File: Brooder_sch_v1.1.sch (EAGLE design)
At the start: 37 parts, among them J2 1X2-3.5MM, J4 1X2-3.5MM, T1 2N2222, U1 328P

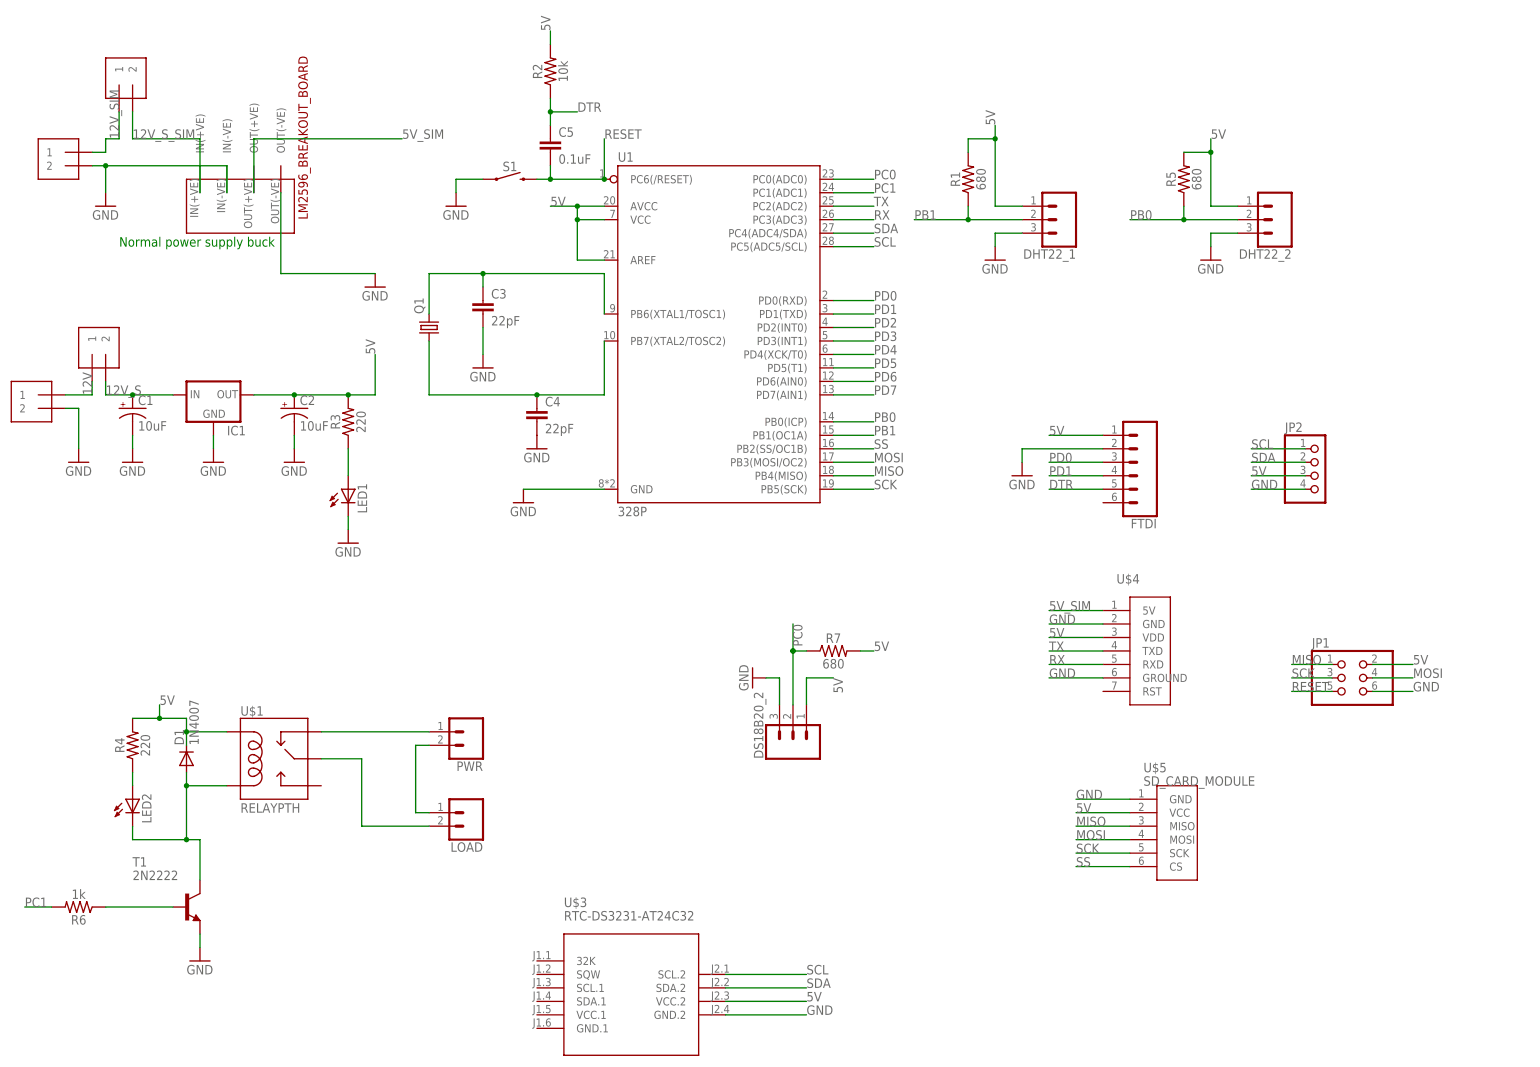
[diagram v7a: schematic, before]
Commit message: Switches the signal and ground signals for all the sensors
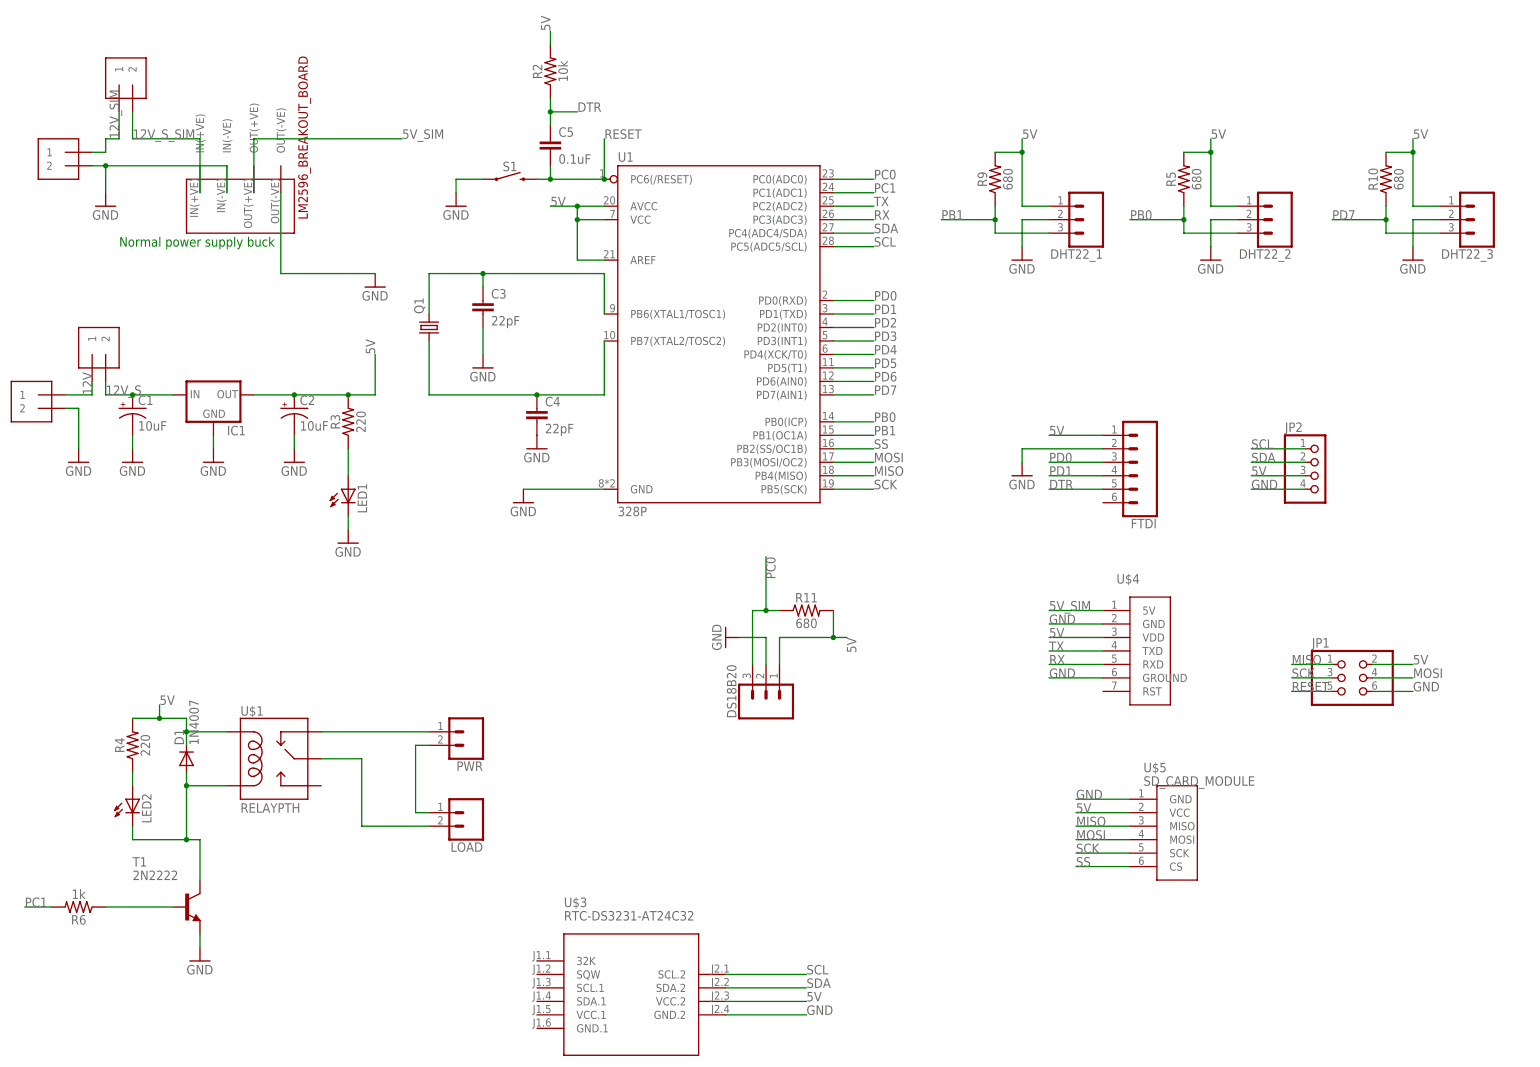
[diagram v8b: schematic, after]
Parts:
- removed DS18B20_2: 455-1750-1-ND, SparkFun-Connectors:CONN_03
- removed R1, R7: 680, SparkFun-Resistors:10MOHM-HORIZ-1/4W-5%
- added DHT22_3, DS18B20: 455-1750-1-ND, SparkFun-Connectors:CONN_03
- added R10, R11, R9: 680, SparkFun-Resistors:10MOHM-HORIZ-1/4W-5%
- DHT22_1: value dht22_1 -> 455-1750-1-ND
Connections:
- net 5V: now also DHT22_3.1, DS18B20.1, R10.2, R11.2, R9.2; no longer DS18B20_2.1, R1.2, R7.2
- net GND: now also DHT22_1.2, DHT22_2.2, DHT22_3.2, DS18B20.2; no longer DHT22_1.3, DHT22_2.3, DS18B20_2.3
- net PB0: now also DHT22_2.3; no longer DHT22_2.2
- net PB1: now also DHT22_1.3, R9.1; no longer DHT22_1.2, R1.1
- net PC0: now also DS18B20.3, R11.1; no longer DS18B20_2.2, R7.1
- net PD7: now also DHT22_3.3, R10.1
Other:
- moved on the sheet: DHT22_1
